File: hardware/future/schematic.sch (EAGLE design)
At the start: 86 parts, among them IC1 SCANTOOL, IC2 LM339PWR, IC3 LM339PWR, IC4 MCP2551, Q2 BSS138, Q3 MMBT2222, Q4 MMBT2222, Q6 BSS138, Q7 ZXMP6A13FTA, Q8 MMBT2222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

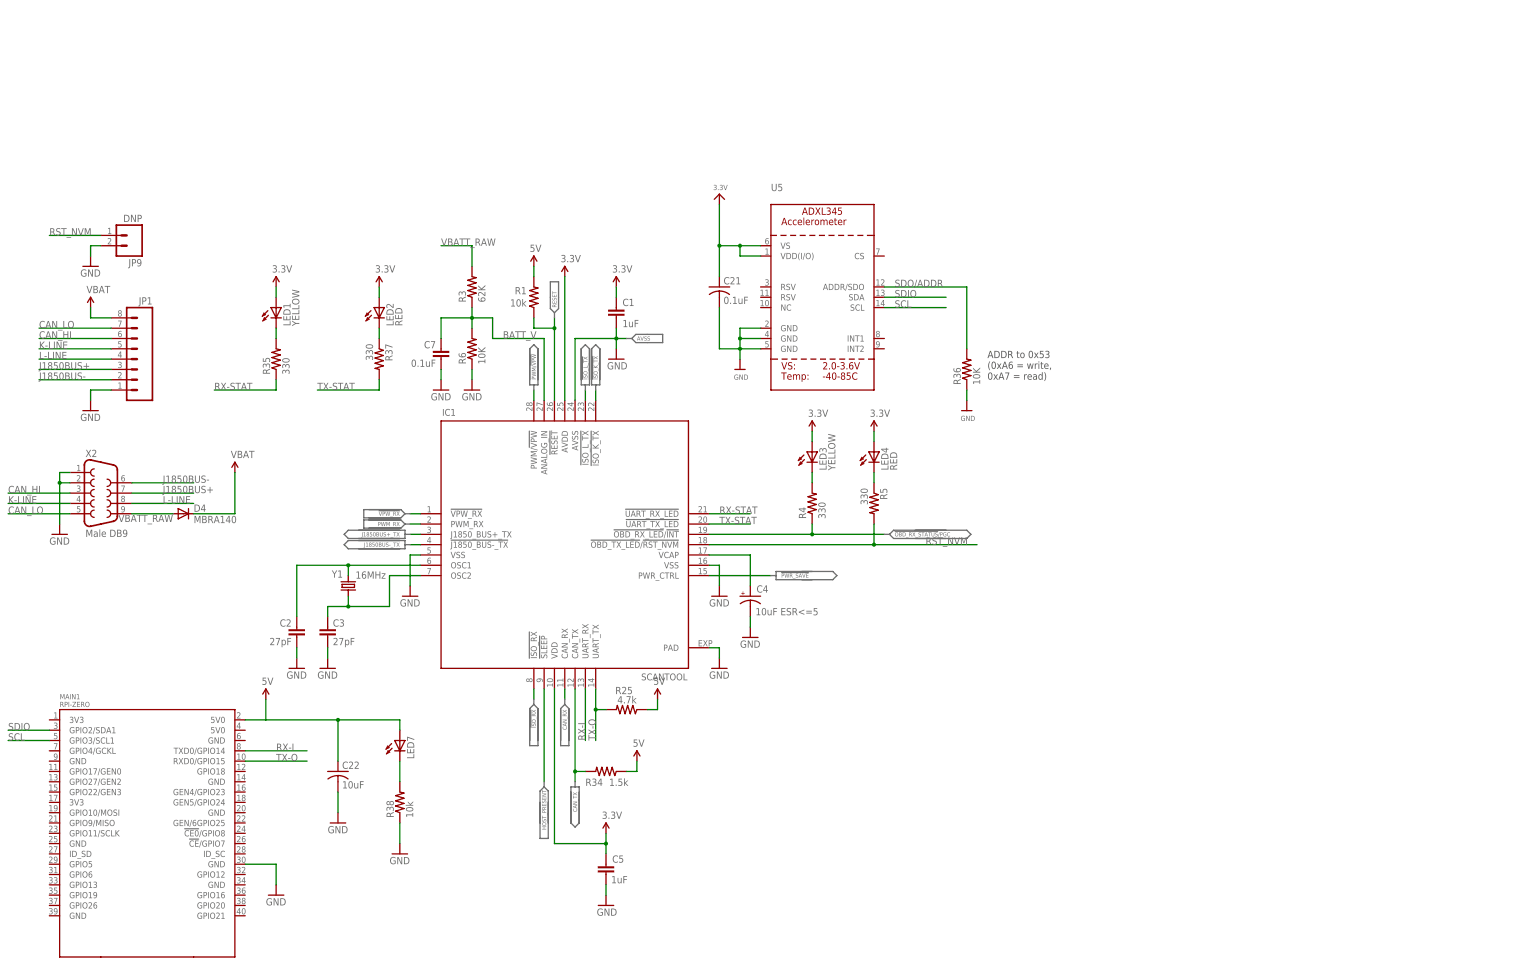
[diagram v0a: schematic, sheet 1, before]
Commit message: android app plus updated board
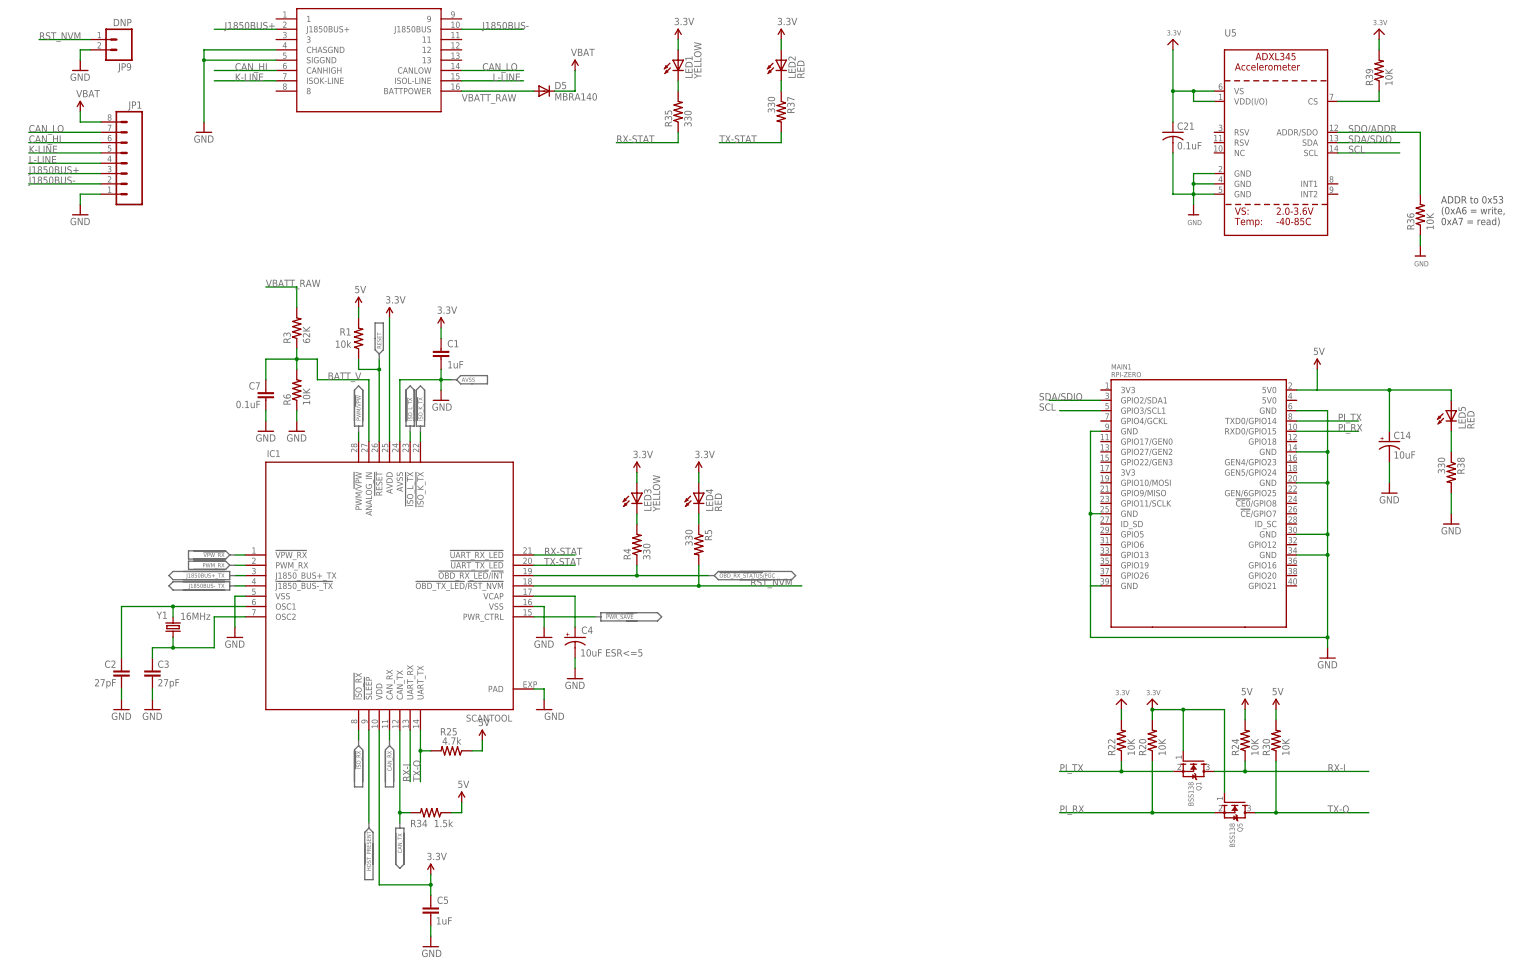
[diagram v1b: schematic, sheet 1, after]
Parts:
- removed C22: 10uF, adafruit:C-US050-025X075
- removed D4: MBRA140, SparkFun:DIODESMA
- removed LED7: (no value), adafruit:LED3MM
- removed X2: Male DB9, SparkFun:DB9MALE
- added C14: 10uF, SparkFun:CAP_POL1206
- added D5: MBRA140, SparkFun:DIODESMA
- added LED5: RED, SparkFun:LED0603
- added OBD_CONN: OBDII, SparkFun-Connectors:OBDII
- added Q1, Q5: BSS138, microbuilder:MOSFET-NWIDE
- added R20, R22, R24, R30, R39: 10K, adafruit:R-US_R0805
- R38: value 10k -> 330; device resistor:R-US_R0805 -> SparkFun:RESISTOR0402-RES
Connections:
- net SDIO renamed SDA/SDIO
- new net N$2: R39.1, U5.CS
- new net PI_RX: MAIN1.RXD0/GPIO15, Q5.S, R20.1
- new net PI_TX: MAIN1.TXD0/GPIO14, Q1.S, R22.1
- net 3.3V: now also Q1.G, Q5.G, R20.2, R22.2, R39.2
- net 5V: now also C14.+, LED5.A, R24.2, R30.2; no longer C22.1, LED7.A
- net CAN_HI: now also OBD_CONN.CANHIGH; no longer X2.3
- net CAN_LO: now also OBD_CONN.CANLOW; no longer X2.5
- net GND: now also C14.-, MAIN1.GND@1, MAIN1.GND@2, MAIN1.GND@3, MAIN1.GND@4, MAIN1.GND@5, MAIN1.GND@7, MAIN1.GND@8, OBD_CONN.CHASGND, OBD_CONN.SIGGND, R38.2; no longer C22.2, R38.1, X2.1, X2.2
- net J1850BUS+: now also OBD_CONN.J1850BUS+; no longer X2.7
- net J1850BUS-: now also OBD_CONN.J1850BUS; no longer X2.6
- net K-LINE: now also OBD_CONN.ISOK-LINE; no longer X2.4
- net L-LINE: now also OBD_CONN.ISOL-LINE; no longer X2.8
- net N$15: now also LED5.C, R38.1; no longer LED7.C, R38.2
- net RX-I: now also Q1.D, R24.1; no longer MAIN1.TXD0/GPIO14
- net TX-O: now also Q5.D, R30.1; no longer MAIN1.RXD0/GPIO15
- net VBAT: no longer D4.C
- net VBATT_RAW: now also D5.A, OBD_CONN.BATTPOWER; no longer D4.A, X2.9
- net VCC: now also D5.C
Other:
- moved on the sheet: C1, C2, C21, C3, C4, C5, C7, IC1, JP1, JP9, LED1, LED2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

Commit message: future design schematic and layout
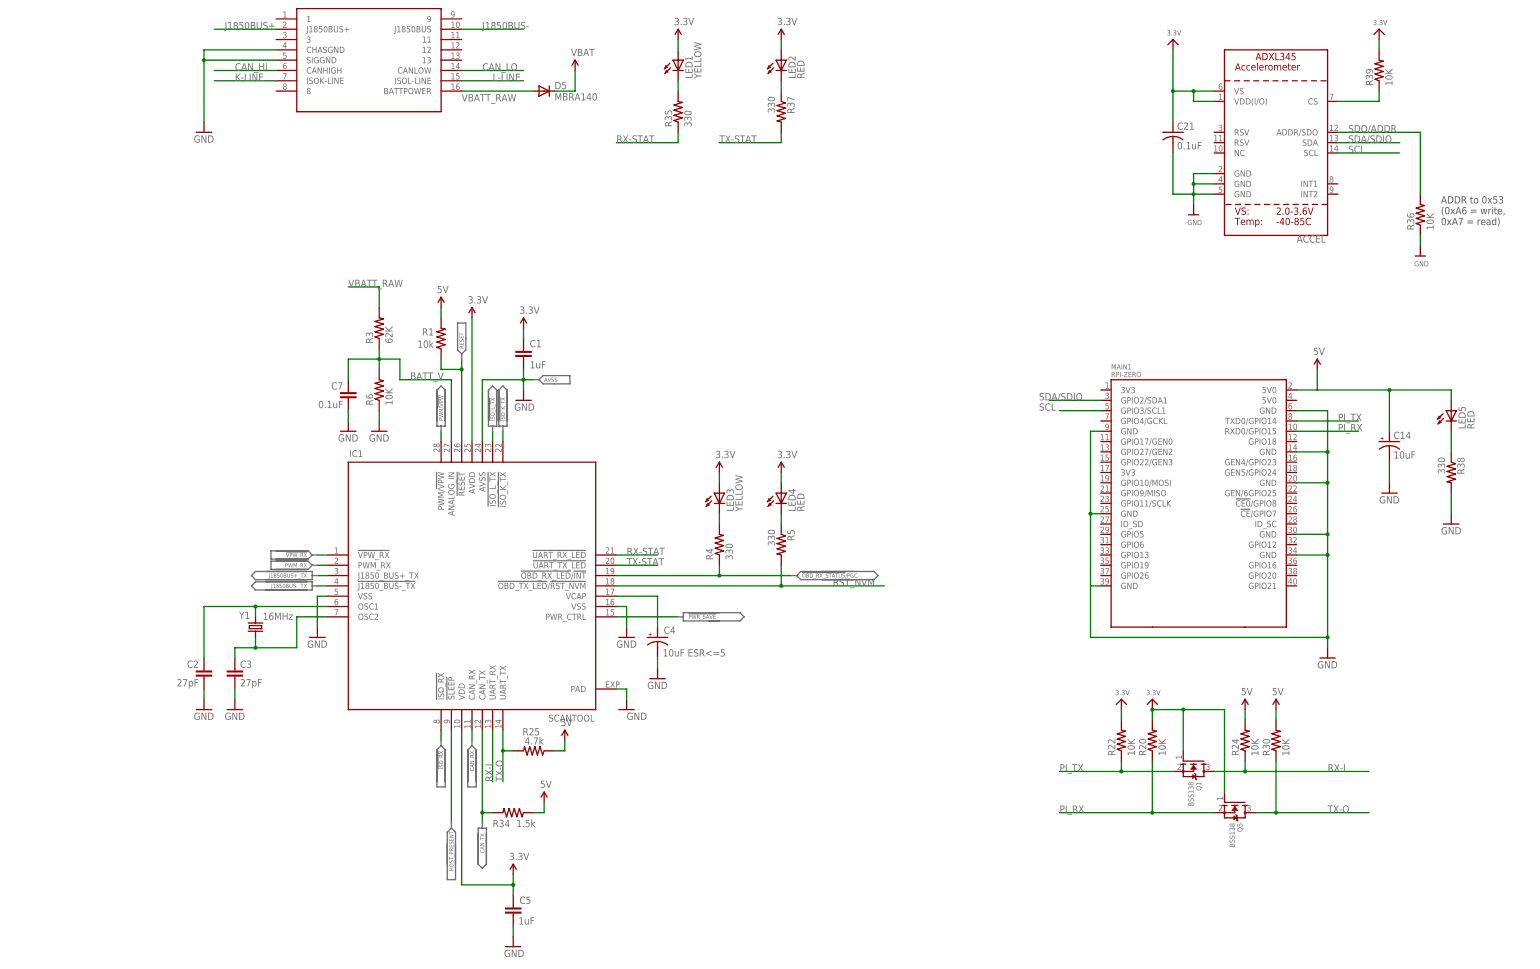
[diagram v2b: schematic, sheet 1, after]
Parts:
- removed JP1: (no value), SparkFun:M08
- removed JP9: DNP, SparkFun:M02PTH
- renumbered U5 to ACCEL
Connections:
- net CAN_HI: no longer JP1.6
- net CAN_LO: no longer JP1.7
- net GND: no longer JP1.1, JP9.2
- net J1850BUS+: no longer JP1.3
- net J1850BUS-: no longer JP1.2
- net K-LINE: no longer JP1.5
- net L-LINE: no longer JP1.4
- net RST_NVM: no longer JP9.1
- net VBAT: no longer JP1.8
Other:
- moved on the sheet: C1, C2, C3, C4, C5, C7, IC1, LED3, LED4, R1, R25, R3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

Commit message: App aesthetic fixes + future board layout
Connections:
- new net VCC/2: C15.+, C16.1, C8.1, R2.1, R26.1, R43.2, U1.OUT, U4.EN, U4.IN
- net VCC: no longer C15.+, C16.1, C8.1, R2.1, R26.1, R43.2, U1.OUT, U4.EN, U4.IN
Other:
- note added: "+5V Power Supply"
- moved on the sheet: C10, C15, C16, C18, C19, C20, C6, C8, C9, LED6, Q2, R26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

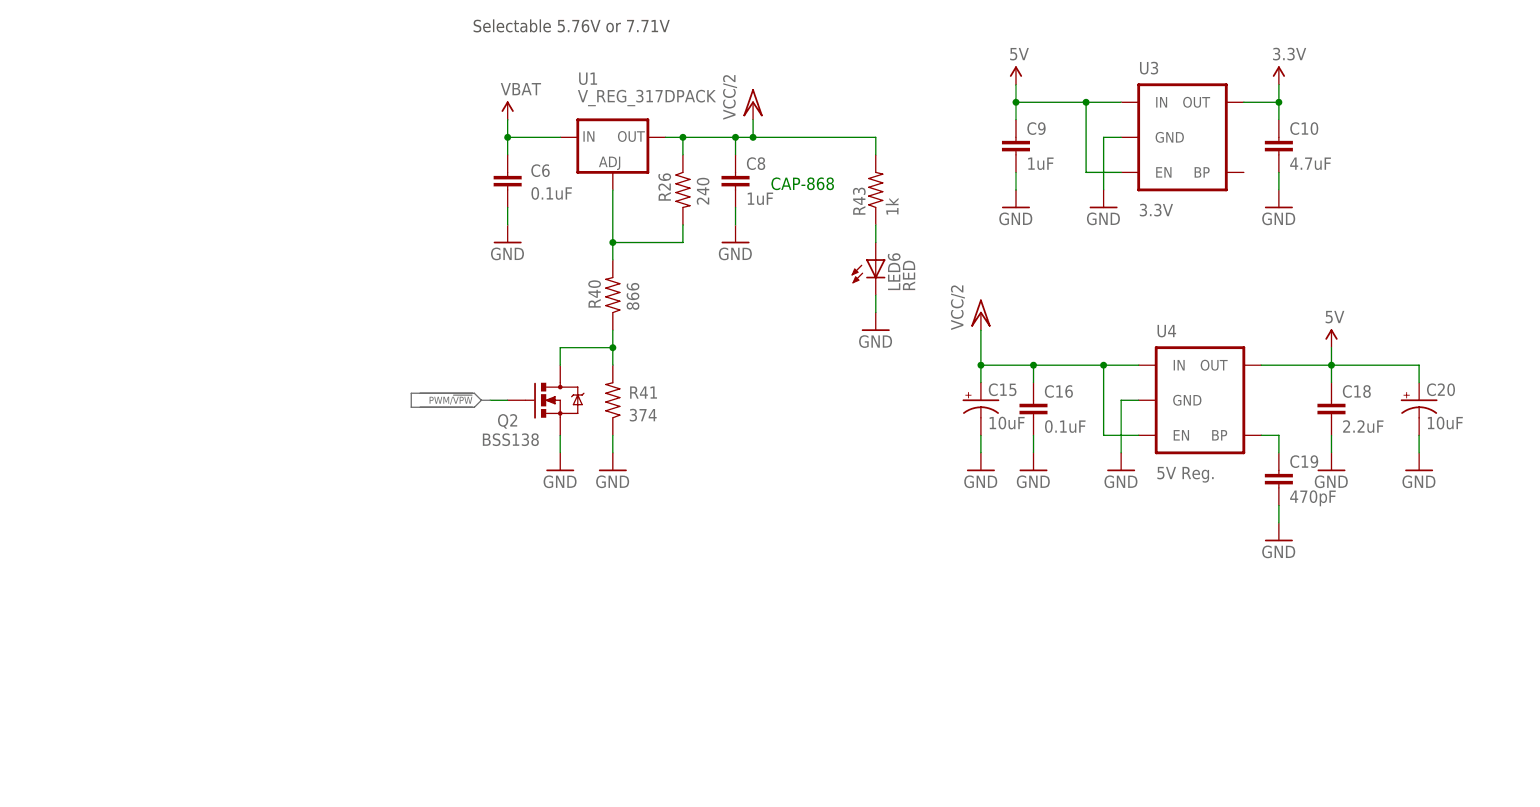
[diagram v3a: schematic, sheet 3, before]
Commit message: minor schematic tweaks
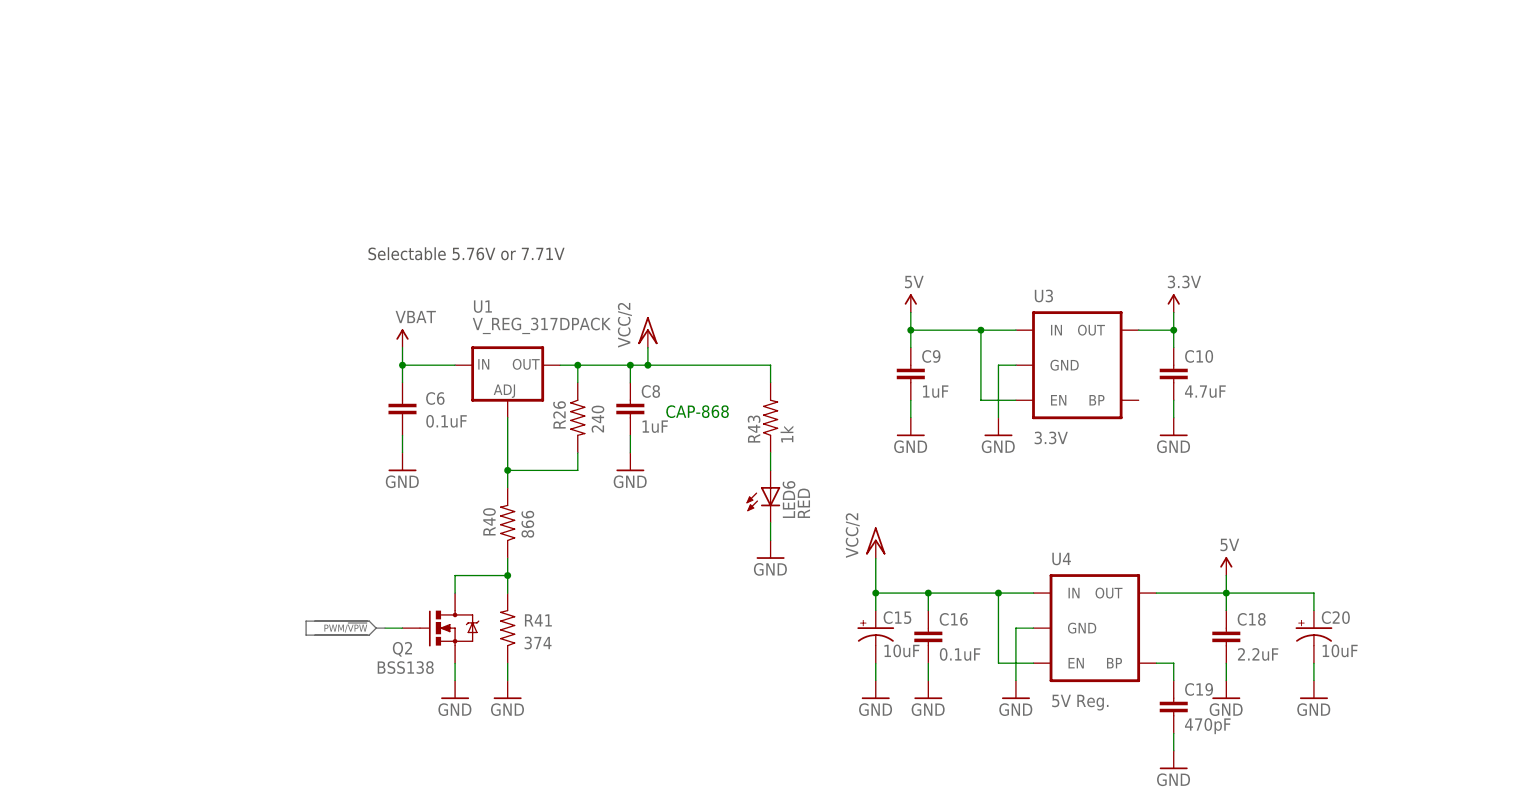
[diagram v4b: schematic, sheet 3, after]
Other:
- moved on the sheet: C10, C15, C16, C18, C19, C20, C6, C8, C9, LED6, Q2, R26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

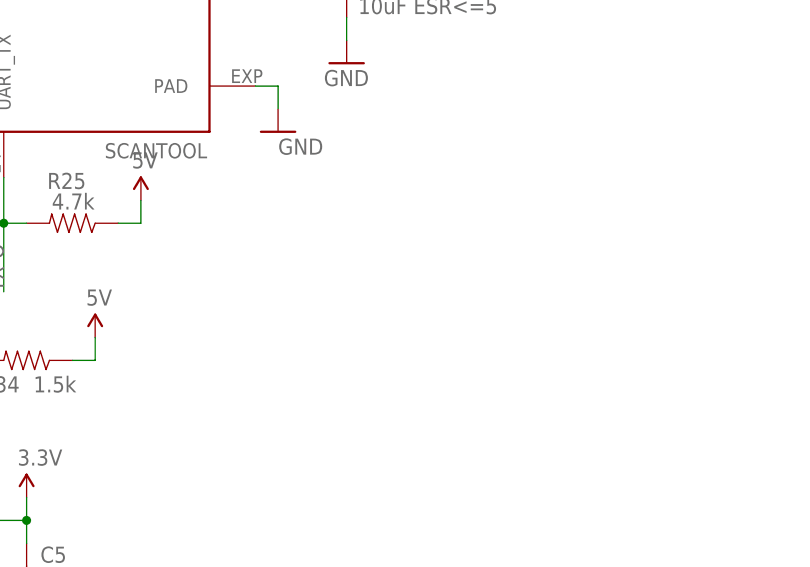
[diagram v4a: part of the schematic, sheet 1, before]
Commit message: added credits in schematic
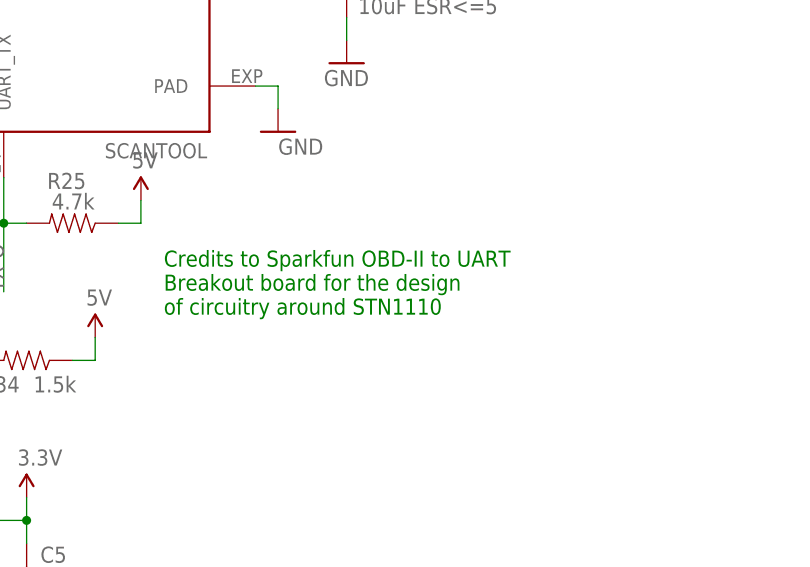
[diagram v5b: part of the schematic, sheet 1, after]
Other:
- note added: "Credits to Sparkfun OBD-II to UART Breakout board for the design of circuitry around STN1110"
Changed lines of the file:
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@@
 <text x="302.26" y="231.14" size="5.08" layer="250" font="vector" ratio="10">Accelerometer</text>
 <text x="269.24" y="154.94" size="5.08" layer="250" font="vector" ratio="10">Raspberry Pi Zero</text>
+<text x="144.78" y="40.64" size="1.778" layer="91">Credits to Sparkfun OBD-II to UART
+Breakout board for the design
+of circuitry around STN1110</text>
 </plain>
 <instances>
